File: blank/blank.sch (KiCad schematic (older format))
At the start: 2 parts

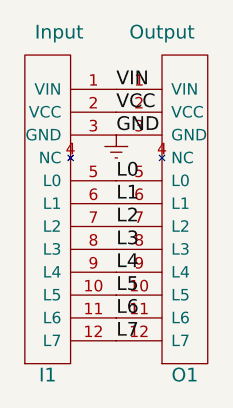
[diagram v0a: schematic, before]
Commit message: More work to ensure there are no errors from KiCAD's schematic checker. Fixed the multiplexer module, so that all 7 slaves will work (only 6 were working, due to a missing VCC to the "Next Output").
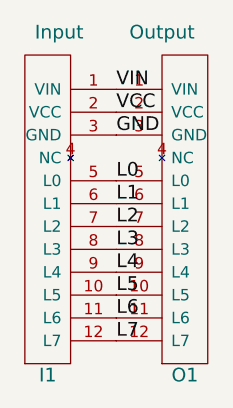
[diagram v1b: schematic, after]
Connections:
- net Earth renamed GND
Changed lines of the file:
@@
 EESchema Schematic File Version 2
-LIBS:blank-rescue
 LIBS:power
 LIBS:device
@@
 LIBS:valves
 LIBS:eplay
-LIBS:Switch
-LIBS:blank-cache
 EELAYER 25 0
 EELAYER END
@@
 L7
 $Comp
-L Earth #PWR01
-U 1 1 5AC24527
-P 2250 2100
-F 0 "#PWR01" H 2250 1850 50  0001 C CNN
-F 1 "Earth" H 2250 1950 50  0001 C CNN
-F 2 "" H 2250 2100 50  0001 C CNN
-F 3 "" H 2250 2100 50  0001 C CNN
-	1    2250 2100
-	1    0    0    -1
-$EndComp
-$Comp
 L Input I1
